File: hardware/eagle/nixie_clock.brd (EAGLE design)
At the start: 171.4 x 78.7 mm, 50 parts, among them IC1 74141N, IC10 7477N, IC11 74141N, IC12 7477N, IC13 74AC11238, IC2 7477N, IC3 74141N, IC4 7477N, IC5 74141N, IC6 7477N, IC7 74141N, IC8 7477N, IC9 74141N, J1_180V 22-27-2021-02, J1_5V1 22-27-2021-02

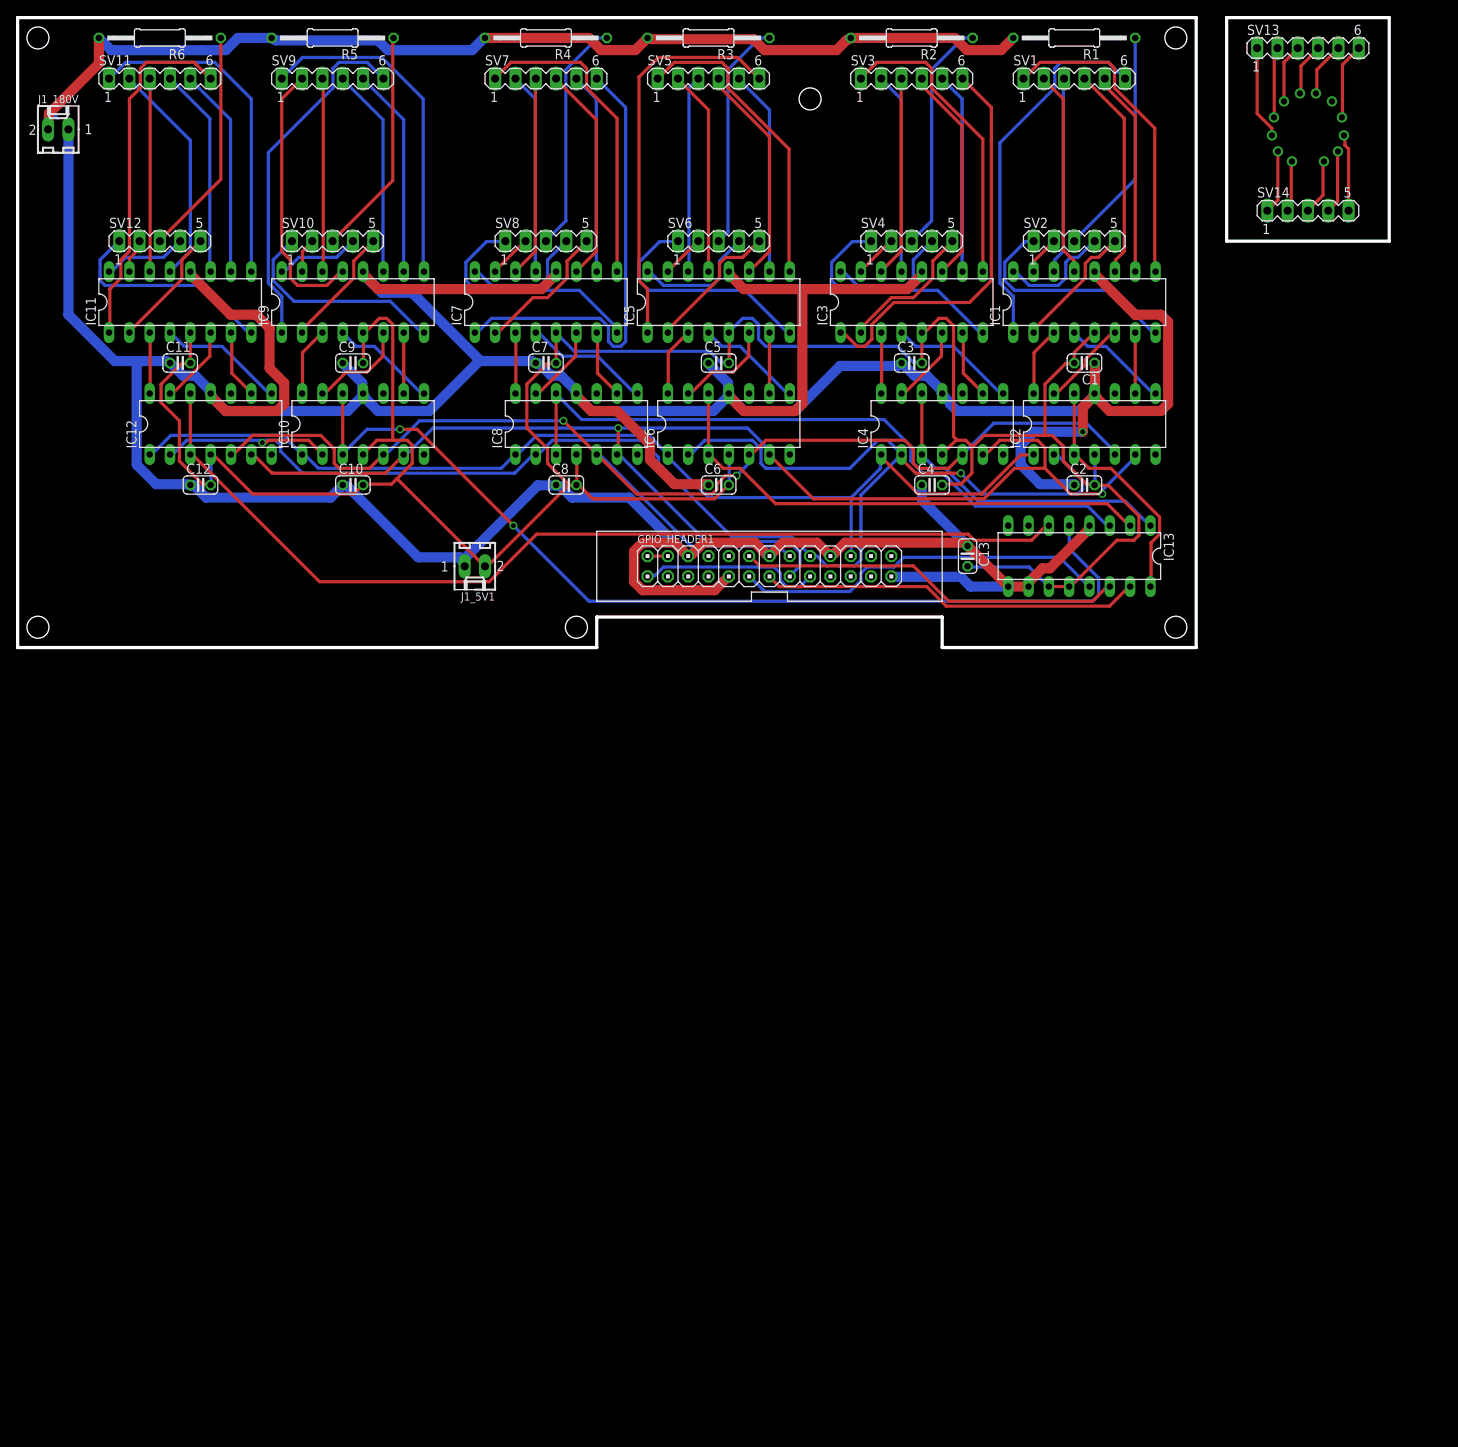
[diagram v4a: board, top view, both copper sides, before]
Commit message: Added power supply on eagle project
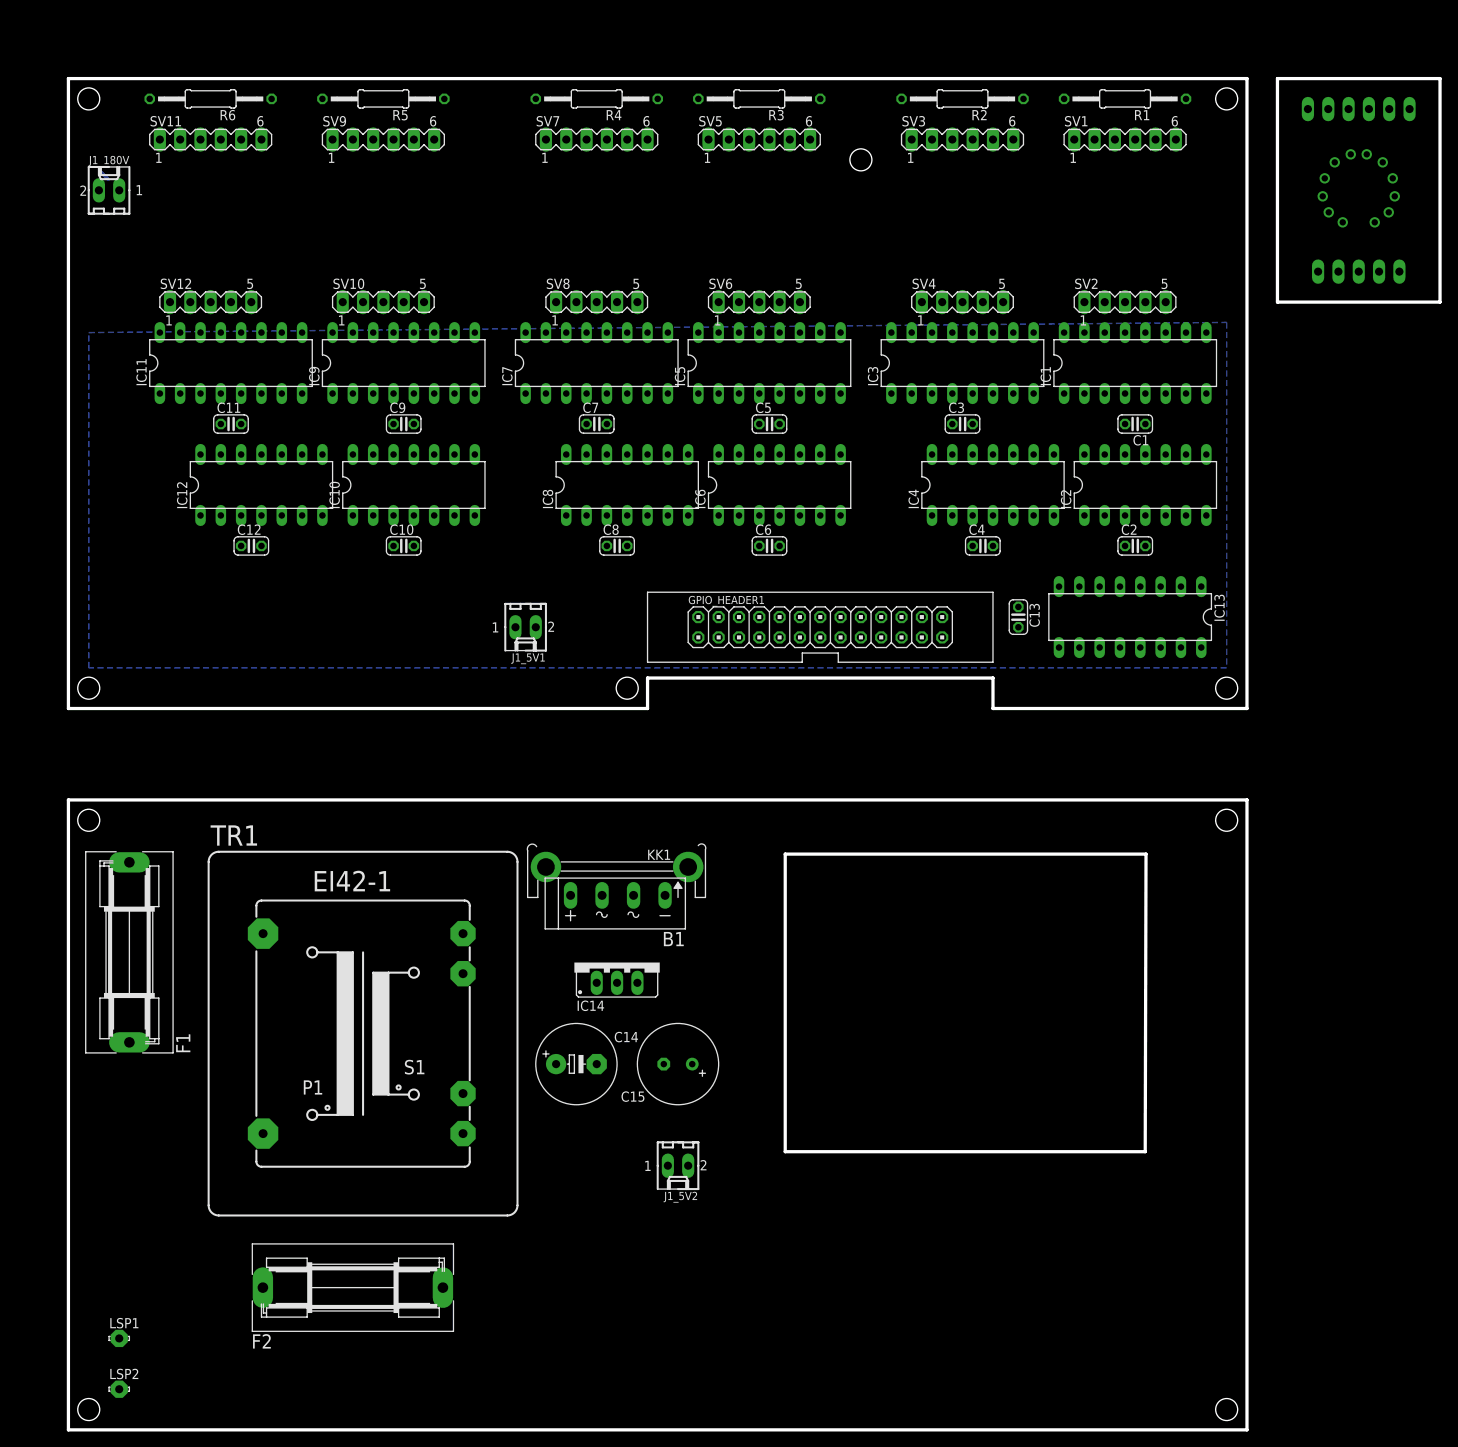
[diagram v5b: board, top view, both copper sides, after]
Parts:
- added B1: (no value), rectifier:FBP1,5
- added C14: (no value), rcl:E5-10,5
- added C15: (no value), rcl:E3,5-10
- added F1, F2: FUSESH22,5A, fuse:SH22,5A
- added IC14: (no value), v-reg:78XXS
- added J1_5V2: 22-27-2021-02, con-molex:6410-02
- added KK1: FK218, heatsink:FK218
- added LSP1, LSP2: LSP10, solpad:LSP10
- added TR1: (no value), trafo:EI42-1
- moved SV2 9.92 mm to (132.1, 50.8)
- moved SV4 9.92 mm to (111.8, 50.8)
- moved SV8 9.92 mm to (66.0, 50.8)
- moved C13 9.92 mm to (118.7, 11.4)
- moved GPIO_HEADER1 9.92 mm to (94.0, 10.2)
- moved IC13 9.92 mm to (132.7, 11.4)
- moved IC6 9.92 mm to (88.9, 27.9)
- moved SV12 9.92 mm to (17.8, 50.8)
- moved J1_180V 9.92 mm to (5.08, 64.8)
- moved C3 9.92 mm to (111.8, 35.6)
- moved C7 9.92 mm to (66.0, 35.6)
- moved C8 9.92 mm to (68.6, 20.3)
- moved IC10 9.92 mm to (43.2, 27.9)
- moved IC3 9.92 mm to (111.8, 43.2)
- moved IC7 9.92 mm to (66.0, 43.2)
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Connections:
- new net N$108: B1.+, C14.+, IC14.IN
- new net N$117: F1.1, LSP1.MP
- new net N$118: F1.2, TR1.1
- new net N$119: LSP2.MP, TR1.5
- new net N$120: F2.1, TR1.9
- new net N$121: B1.AC2, F2.2
- new net N$122: B1.AC1, TR1.7
- new net N$123: C15.+, IC14.OUT, J1_5V2.2
- new net N$125: B1.-, C14.-, C15.-, IC14.GND, J1_5V2.1
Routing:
- net GND: track 603.0 -> 0.00 mm, vias 1 -> 0
- net N$124: track 337.5 -> 0.00 mm
- net N$95: track 185.6 -> 0.00 mm, vias 2 -> 0
- net N$17: track 169.7 -> 0.00 mm, vias 2 -> 0
- net N$94: track 160.3 -> 0.00 mm, vias 2 -> 0
- net VCC: track 134.6 -> 0.00 mm
- net N$96: track 133.1 -> 0.00 mm
- net N$93: track 125.1 -> 0.00 mm
- net N$78: track 122.9 -> 0.00 mm, vias 2 -> 0
- net N$63: track 84.8 -> 0.00 mm
- net N$48: track 64.0 -> 0.00 mm
- net N$64: track 56.7 -> 0.00 mm
- net N$27: track 50.8 -> 0.00 mm
- net N$43: track 49.5 -> 0.00 mm
- net N$98: track 48.2 -> 0.00 mm
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- added copper zone on layer 16, net GND
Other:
- board size 171.4 x 78.7 mm -> 171.4 x 168.9 mm

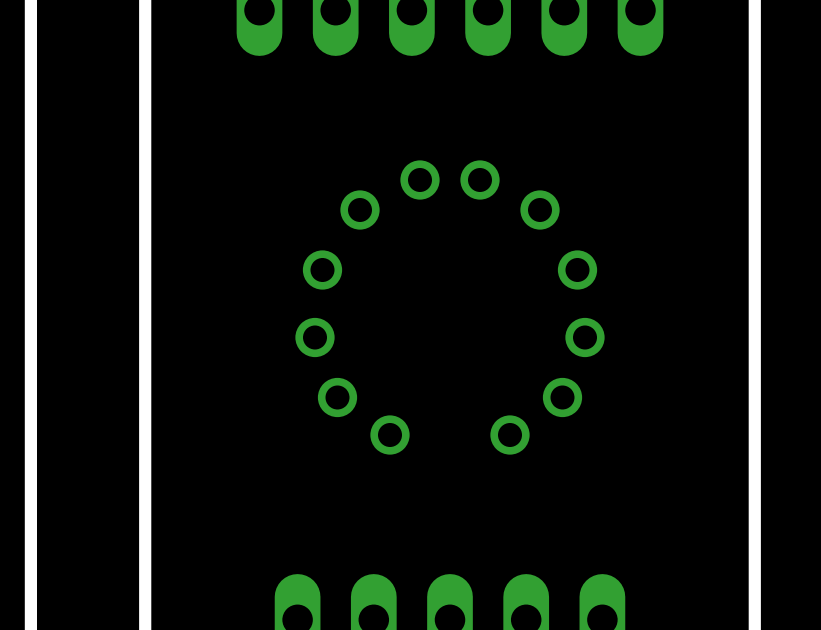
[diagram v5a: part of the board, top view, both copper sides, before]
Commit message: FreeCad nixie model
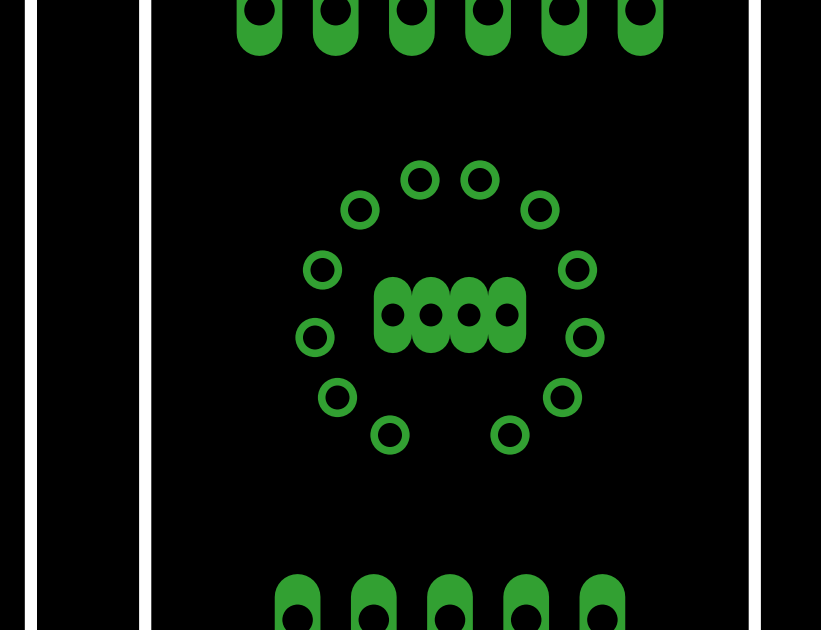
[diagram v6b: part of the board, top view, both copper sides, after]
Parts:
- added D1: LED-RGB-CC-THRUCLEAR, SparkFun-LED:LED-RGB-THRU
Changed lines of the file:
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@@
 <setting verticaltext="up"/>
 </settings>
-<grid distance="0.1" unitdist="mm" unit="mm" style="dots" multiple="1" display="yes" altdistance="0.025" altunitdist="inch" altunit="inch"/>
+<grid distance="1.27" unitdist="mm" unit="mm" style="lines" multiple="1" display="yes" altdistance="0.025" altunitdist="inch" altunit="inch"/>
 <layers>
 <layer number="1" name="Top" color="4" fill="1" visible="yes" active="yes"/>
@@
 <layer number="48" name="Document" color="7" fill="1" visible="no" active="yes"/>
 <layer number="49" name="Reference" color="7" fill="1" visible="no" active="yes"/>
+<layer number="50" name="dxf" color="7" fill="1" visible="no" active="no"/>
 <layer number="51" name="tDocu" color="7" fill="1" visible="no" active="yes"/>
 <layer number="52" name="bDocu" color="7" fill="1" visible="no" active="yes"/>
+<layer number="53" name="tGND_GNDA" color="7" fill="9" visible="no" active="no"/>
+<layer number="54" name="bGND_GNDA" color="1" fill="9" visible="no" active="no"/>
+<layer number="56" name="wert" color="7" fill="1" visible="no" active="no"/>
+<layer number="57" name="tCAD" color="7" fill="1" visible="no" active="no"/>
+<layer number="59" name="tCarbon" color="7" fill="1" visible="no" active="no"/>
+<layer number="60" name="bCarbon" color="7" fill="1" visible="no" active="no"/>
+<layer number="90" name="Modules" color="5" fill="1" visible="no" active="no"/>
 <layer number="91" name="Nets" color="2" fill="1" visible="no" active="no"/>
 <layer number="92" name="Busses" color="1" fill="1" visible="no" active="no"/>
@@
 <layer number="98" name="Guide" color="6" fill="1" visible="no" active="no"/>
 <layer number="99" name="SpiceOrder" color="5" fill="1" visible="no" active="no"/>
+<layer number="100" name="Muster" color="7" fill="1" visible="no" active="no"/>
+<layer number="101" name="Patch_Top" color="12" fill="4" visible="yes" active="yes"/>
+<layer number="102" name="Vscore" color="7" fill="1" visible="yes" active="yes"/>
+<layer number="103" name="tMap" color="7" fill="1" visible="yes" active="yes"/>
+<layer number="104" name="Name" color="16" fill="1" visible="yes" active="yes"/>
+<layer number="105" name="tPlate" color="7" fill="1" visible="yes" active="yes"/>
+<layer number="106" name="bPlate" color="7" fill="1" visible="yes" active="yes"/>
+<layer number="107" name="Crop" color="7" fill="1" visible="yes" active="yes"/>
+<layer number="108" name="tplace-old" color="10" fill="1" visible="yes" active="yes"/>
+<layer number="109" name="ref-old" color="11" fill="1" visible="yes" active="yes"/>
+<layer number="110" name="fp0" color="7" fill="1" visible="yes" active="yes"/>
+<layer number="111" name="LPC17xx" color="7" fill="1" visible="yes" active="yes"/>
+<layer number="112" name="tSilk" color="7" fill="1" visible="yes" active="yes"/>
+<layer number="113" name="IDFDebug" color="4" fill="1" visible="yes" active="yes"/>
+<layer number="116" name="Patch_BOT" color="9" fill="4" visible="yes" active="yes"/>
+<layer number="118" name="Rect_Pads" color="7" fill="1" visible="yes" active="yes"/>
+<layer number="121" name="_tsilk" color="7" fill="1" visible="yes" active="yes"/>
+<layer number="122" name="_bsilk" color="7" fill="1" visible="yes" active="yes"/>
+<layer number="123" name="tTestmark" color="7" fill="1" visible="yes" active="yes"/>
+<layer number="124" name="bTestmark" color="7" fill="1" visible="yes" active="yes"/>
+<layer number="125" name="_tNames" color="7" fill="1" visible="yes" active="yes"/>
+<layer number="126" name="_bNames" color="7" fill="1" visible="yes" active="yes"/>
+<layer number="127" name="_tValues" color="7" fill="1" visible="yes" active="yes"/>
+<layer number="128" name="_bValues" color="7" fill="1" visible="yes" active="yes"/>
+<layer number="129" name="Mask" color="7" fill="1" visible="yes" active="yes"/>
+<layer number="131" name="tAdjust" color="7" fill="1" visible="yes" active="yes"/>
+<layer number="132" name="bAdjust" color="7" fill="1" visible="yes" active="yes"/>
+<layer number="144" name="Drill_legend" color="7" fill="1" visible="yes" active="yes"/>
+<layer number="150" name="Notes" color="7" fill="1" visible="yes" active="yes"/>
+<layer number="151" name="HeatSink" color="7" fill="1" visible="yes" active="yes"/>
+<layer number="152" name="_bDocu" color="7" fill="1" visible="yes" active="yes"/>
+<layer number="153" name="FabDoc1" color="7" fill="1" visible="yes" active="yes"/>
+<layer number="154" name="FabDoc2" color="7" fill="1" visible="yes" active="yes"/>
+<layer number="155" name="FabDoc3" color="7" fill="1" visible="yes" active="yes"/>
+<layer number="199" name="Contour" color="7" fill="1" visible="yes" active="yes"/>
+<layer number="200" name="200bmp" color="1" fill="10" visible="yes" active="yes"/>
+<layer number="201" name="201bmp" color="2" fill="10" visible="yes" active="yes"/>
+<layer number="202" name="202bmp" color="3" fill="10" visible="yes" active="yes"/>
+<layer number="203" name="203bmp" color="4" fill="10" visible="yes" active="yes"/>
+<layer number="204" name="204bmp" color="5" fill="10" visible="yes" active="yes"/>
+<layer number="205" name="205bmp" color="6" fill="10" visible="yes" active="yes"/>
+<layer number="206" name="206bmp" color="7" fill="10" visible="yes" active="yes"/>
+<layer number="207" name="207bmp" color="8" fill="10" visible="yes" active="yes"/>
+<layer number="208" name="208bmp" color="9" fill="10" visible="yes" active="yes"/>
+<layer number="209" name="209bmp" color="7" fill="1" visible="yes" active="yes"/>
+<layer number="210" name="210bmp" color="7" fill="1" visible="yes" active="yes"/>
+<layer number="211" name="211bmp" color="7" fill="1" visible="yes" active="yes"/>
+<layer number="212" name="212bmp" color="7" fill="1" visible="yes" active="yes"/>
+<layer number="213" name="213bmp" color="7" fill="1" visible="yes" active="yes"/>
+<layer number="214" name="214bmp" color="7" fill="1" visible="yes" active="yes"/>
+<layer number="215" name="215bmp" color="7" fill="1" visible="yes" active="yes"/>
+<layer number="216" name="216bmp" color="7" fill="1" visible="yes" active="yes"/>
+<layer number="217" name="217bmp" color="18" fill="1" visible="no" active="no"/>
+<layer number="218" name="218bmp" color="19" fill="1" visible="no" active="no"/>
+<layer number="219" name="219bmp" color="20" fill="1" visible="no" active="no"/>
+<layer number="220" name="220bmp" color="21" fill="1" visible="no" active="no"/>
+<layer number="221" name="221bmp" color="22" fill="1" visible="no" active="no"/>
+<layer number="222" name="222bmp" color="23" fill="1" visible="no" active="no"/>
+<layer number="223" name="223bmp" color="24" fill="1" visible="no" active="no"/>
+<layer number="224" name="224bmp" color="25" fill="1" visible="no" active="no"/>
+<layer number="225" name="225bmp" color="7" fill="1" visible="yes" active="yes"/>
+<layer number="226" name="226bmp" color="7" fill="1" visible="yes" active="yes"/>
+<layer number="227" name="227bmp" color="7" fill="1" visible="yes" active="yes"/>
+<layer number="228" name="228bmp" color="7" fill="1" visible="yes" active="yes"/>
+<layer number="229" name="229bmp" color="7" fill="1" visible="yes" active="yes"/>
+<layer number="230" name="230bmp" color="7" fill="1" visible="yes" active="yes"/>
+<layer number="231" name="231bmp" color="7" fill="1" visible="yes" active="yes"/>
+<layer number="248" name="Housing" color="7" fill="1" visible="yes" active="yes"/>
+<layer number="249" name="Edge" color="7" fill="1" visible="yes" active="yes"/>
+<layer number="250" name="Descript" color="3" fill="1" visible="no" active="no"/>
+<layer number="251" name="SMDround" color="12" fill="11" visible="no" active="no"/>
+<layer number="254" name="cooling" color="7" fill="1" visible="yes" active="yes"/>
+<layer number="255" name="routoute" color="7" fill="1" visible="yes" active="yes"/>
 </layers>
 <board>
@@
 <attribute name="OC_FARNELL" value="unknown" x="76.2" y="-57.15" size="1.778" layer="27" rot="R180" display="off"/>
 </element>
+<element name="D1" library="SparkFun-LED" package="LED-RGB-THRU" value="LED-RGB-CC-THRUCLEAR" x="161.29" y="64.77" rot="MR0">
+<attribute name="PROD_ID" value="DIO-08418" x="161.29" y="64.77" size="1.778" layer="28" rot="MR0" display="off"/>
+</element>
 </elements>
